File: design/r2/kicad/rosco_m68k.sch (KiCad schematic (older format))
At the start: 0 parts

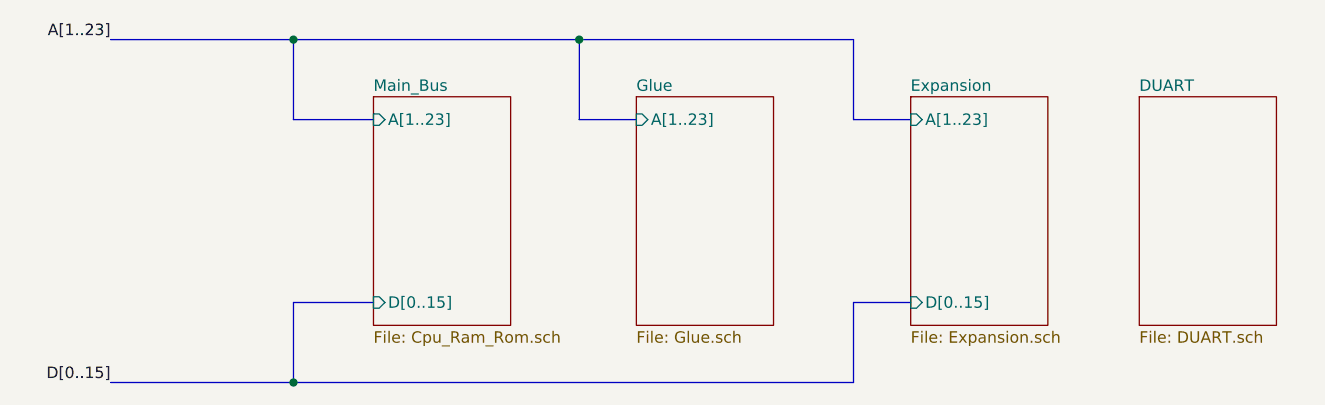
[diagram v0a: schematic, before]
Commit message: Complete schematic capture for r2
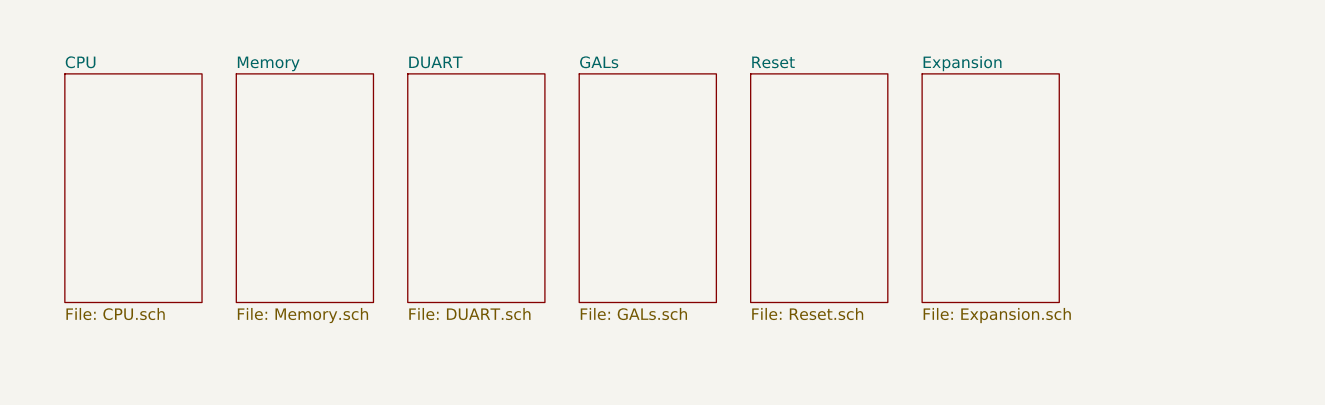
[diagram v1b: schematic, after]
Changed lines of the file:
@@
 $Descr A4 11693 8268
 encoding utf-8
-Sheet 1 5
+Sheet 1 7
 Title "ROSCO_M68K GENERAL PURPOSE MC68010 COMPUTER"
 Date "2021-10-08"
@@
 $EndDescr
 $Sheet
-S 5250 3300 600  1000
-U 5E53B4B8
-F0 "Main_Bus" 50
-F1 "Cpu_Ram_Rom.sch" 50
-F2 "D[0..15]" I L 5250 4200 50
-F3 "A[1..23]" I L 5250 3400 50
-$EndSheet
-$Sheet
-S 6400 3300 600  1000
-U 5E53B952
-F0 "Glue" 50
-F1 "Glue.sch" 50
-F2 "A[1..23]" I L 6400 3400 50
-$EndSheet
-$Sheet
-S 7600 3300 600  1000
+S 7650 3200 600  1000
 U 5E53BC83
 F0 "Expansion" 50
 F1 "Expansion.sch" 50
-F2 "D[0..15]" I L 7600 4200 50
-F3 "A[1..23]" I L 7600 3400 50
 $EndSheet
-Text Label 4100 4550 2    50   ~ 0
-D[0..15]
-Text Label 4100 3050 2    50   ~ 0
-A[1..23]
-Wire Bus Line
-	5250 4200 4900 4200
-Wire Bus Line
-	4100 3050 4900 3050
-Wire Bus Line
-	4900 3050 4900 3400
-Wire Bus Line
-	4900 3400 5250 3400
-Wire Bus Line
-	4900 3050 6150 3050
-Wire Bus Line
-	6150 3050 6150 3400
-Wire Bus Line
-	6150 3400 6400 3400
-Connection ~ 4900 3050
-Wire Bus Line
-	6150 3050 7350 3050
-Wire Bus Line
-	7350 3050 7350 3400
-Wire Bus Line
-	7350 3400 7600 3400
-Connection ~ 6150 3050
-Wire Bus Line
-	4100 4550 4900 4550
-Wire Bus Line
-	4900 4200 4900 4550
-Wire Bus Line
-	7350 4550 4900 4550
-Wire Bus Line
-	7350 4200 7600 4200
-Wire Bus Line
-	7350 4200 7350 4550
-Connection ~ 4900 4550
 $Sheet
-S 8600 3300 600  1000
+S 5400 3200 600  1000
 U 61622E90
 F0 "DUART" 50
 F1 "DUART.sch" 50
 $EndSheet
+$Sheet
+S 6900 3200 600  1000
+U 6162E38E
+F0 "Reset" 50
+F1 "Reset.sch" 50
+$EndSheet
+$Sheet
+S 3900 3200 600  1000
+U 5E53B4B8
+F0 "CPU" 50
+F1 "CPU.sch" 50
+$EndSheet
+$Sheet
+S 4650 3200 600  1000
+U 616B7C9B
+F0 "Memory" 50
+F1 "Memory.sch" 50
+$EndSheet
+$Sheet
+S 6150 3200 600  1000
+U 617D19F3
+F0 "GALs" 50
+F1 "GALs.sch" 50
+$EndSheet
 $EndSCHEMATC
